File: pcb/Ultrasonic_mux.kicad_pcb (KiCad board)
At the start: 2 copper layers, 199.4 x 99.1 mm, 70 parts, among them J0 DB9_Male, J1 DB9_Male, J10 Conn_01x03_Male, J11 Conn_01x03_Male, J12 Conn_01x03_Male, J13 Conn_01x03_Male, J14 Conn_01x03_Male, J15 Conn_01x03_Male, J2 DB9_Male, J3 DB9_Male, J4 DB9_Male, J5 DB9_Male, P1 , P12 , P27 , P28 , P3 , P5 , Q0 MMBT3904, Q1 MMBT3904, Q2 MMBT3904, Q3 MMBT3904, Q4 MMBT3904, Q5 MMBT3904, U1 FeatherM0

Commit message: Organized layout.
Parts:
- moved R2 41.3 mm to (125.0, 78.7)
- moved D22 37.3 mm to (248.9, 78.2), turned to 90 degrees
- moved R3 34.6 mm to (136.1, 83.8), turned to 90 degrees
- moved D31 30.8 mm to (131.1, 135.6), turned to 270 degrees
- moved D2 30.4 mm to (136.1, 77.7), turned to 90 degrees
- moved Q0 29.5 mm to (118.4, 79.2), turned to 180 degrees
- moved R33 26.0 mm to (135.1, 130.0), turned to 270 degrees
- moved P1 23.2 mm to (112.8, 118.9)
- moved D51 23.2 mm to (243.8, 134.1), turned to 270 degrees
- moved R32 22.9 mm to (125.0, 134.1)
- moved D0 22.5 mm to (113.3, 79.2)
- moved D52 20.1 mm to (247.9, 134.6), turned to 270 degrees
- moved D32 19.3 mm to (135.1, 135.6), turned to 270 degrees
- moved D41 19.1 mm to (187.5, 135.1), turned to 270 degrees
- moved +5Vp1 19.1 mm to (119.4, 105.7)
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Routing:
- net GNDPWR: track 41.9 -> 257.1 mm
- net +3V3: track 5.18 -> 29.6 mm
- net Net-(D20-Pad1): track 0.00 -> 22.1 mm
- net Net-(D0-Pad1): track 0.00 -> 21.4 mm
- net Net-(J0-Pad2): track 0.00 -> 20.3 mm
- net Net-(J2-Pad2): track 0.00 -> 20.2 mm
- net Net-(D30-Pad1): track 0.00 -> 18.2 mm
- net Net-(J3-Pad2): track 0.00 -> 18.1 mm
- net Net-(J4-Pad2): track 0.00 -> 17.3 mm
- net Net-(D40-Pad1): track 0.00 -> 16.9 mm
- net Net-(J5-Pad2): track 0.00 -> 16.8 mm
- net Net-(D50-Pad1): track 0.00 -> 15.9 mm
- net RX0: track 0.00 -> 6.46 mm
- net Net-(D41-Pad1): track 0.00 -> 6.34 mm
- net Net-(D51-Pad1): track 0.00 -> 5.83 mm
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
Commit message: Hopefully finished track routes.
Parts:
- +3V3p1, +5Vp1, GNDp1: footprint Pin_Headers:Pin_Header_Angled_1x01_Pitch2.54mm -> Pin_Headers:Pin_Header_Straight_1x01_Pitch2.54mm
- moved GNDp1 151.6 mm to (265.2, 59.4), turned to 180 degrees
- moved +3V3p1 150.1 mm to (260.6, 59.4), turned to 180 degrees
- moved +5Vp1 144.3 mm to (256.0, 59.4), turned to 180 degrees
- moved P1 28.2 mm to (135.1, 101.6)
- moved P12 24.6 mm to (135.1, 113.8)
- moved P3 23.8 mm to (135.1, 105.7)
- moved P27 22.4 mm to (135.1, 97.5)
- moved P28 22.4 mm to (135.1, 92.5)
- moved P5 22.4 mm to (135.1, 109.7)
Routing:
- net +3V3: track 29.6 -> 605.8 mm, vias 0 -> 6
- net GNDPWR: track 257.1 -> 803.0 mm, vias 0 -> 1
- net +5V: track 0.00 -> 532.4 mm
- net RX3: track 4.76 -> 163.9 mm, vias 0 -> 2
- net TRG5: track 0.00 -> 123.5 mm, vias 0 -> 2
- net RX5: track 4.76 -> 118.1 mm, vias 0 -> 2
- net TRG3: track 0.00 -> 111.9 mm, vias 0 -> 4
- net TRG0: track 0.00 -> 110.4 mm, vias 0 -> 3
- net IND5: track 0.00 -> 106.2 mm, vias 0 -> 1
- net IND3: track 0.00 -> 101.1 mm, vias 0 -> 4
- net TRG2: track 0.00 -> 100.2 mm
- net RX0: track 6.46 -> 100.9 mm, vias 0 -> 4
- net RX2: track 5.75 -> 97.6 mm, vias 0 -> 2
- net IND2: track 0.00 -> 83.1 mm, vias 0 -> 1
- net Net-(P12-Pad1): track 0.00 -> 78.5 mm, vias 0 -> 3
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
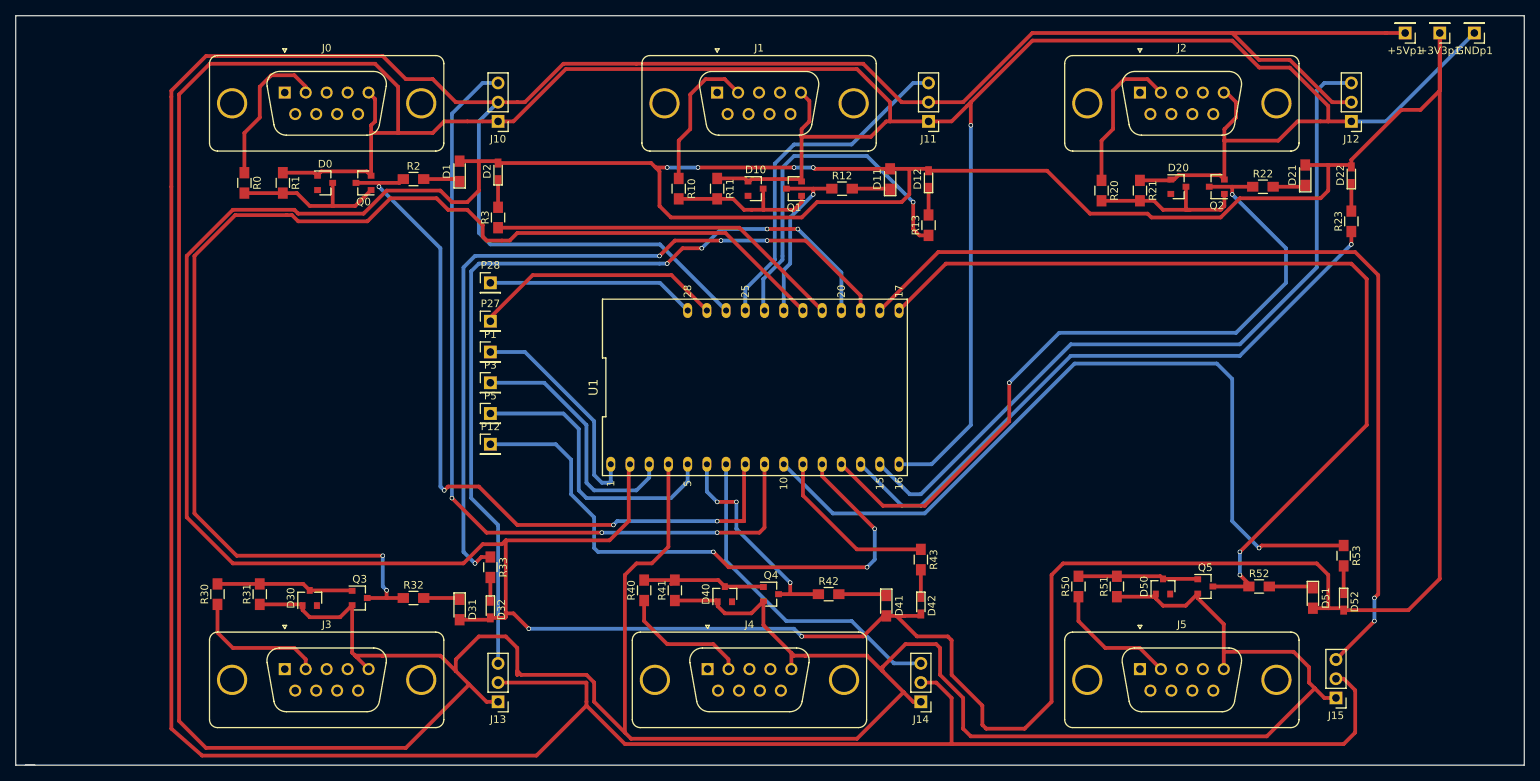
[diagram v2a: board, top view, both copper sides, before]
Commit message: BD: Reduced board size to 150x100mm for easier fit on 'bot, and reduced mechanical stress. Added vias to permit easier mods (runner cuts and soldered wire reconnect to another pad/circuit)
It still thinks 5v is not connected!
Tried replacing connecting segments to J13 and U1
Tried adding another trace to each on bottom of board
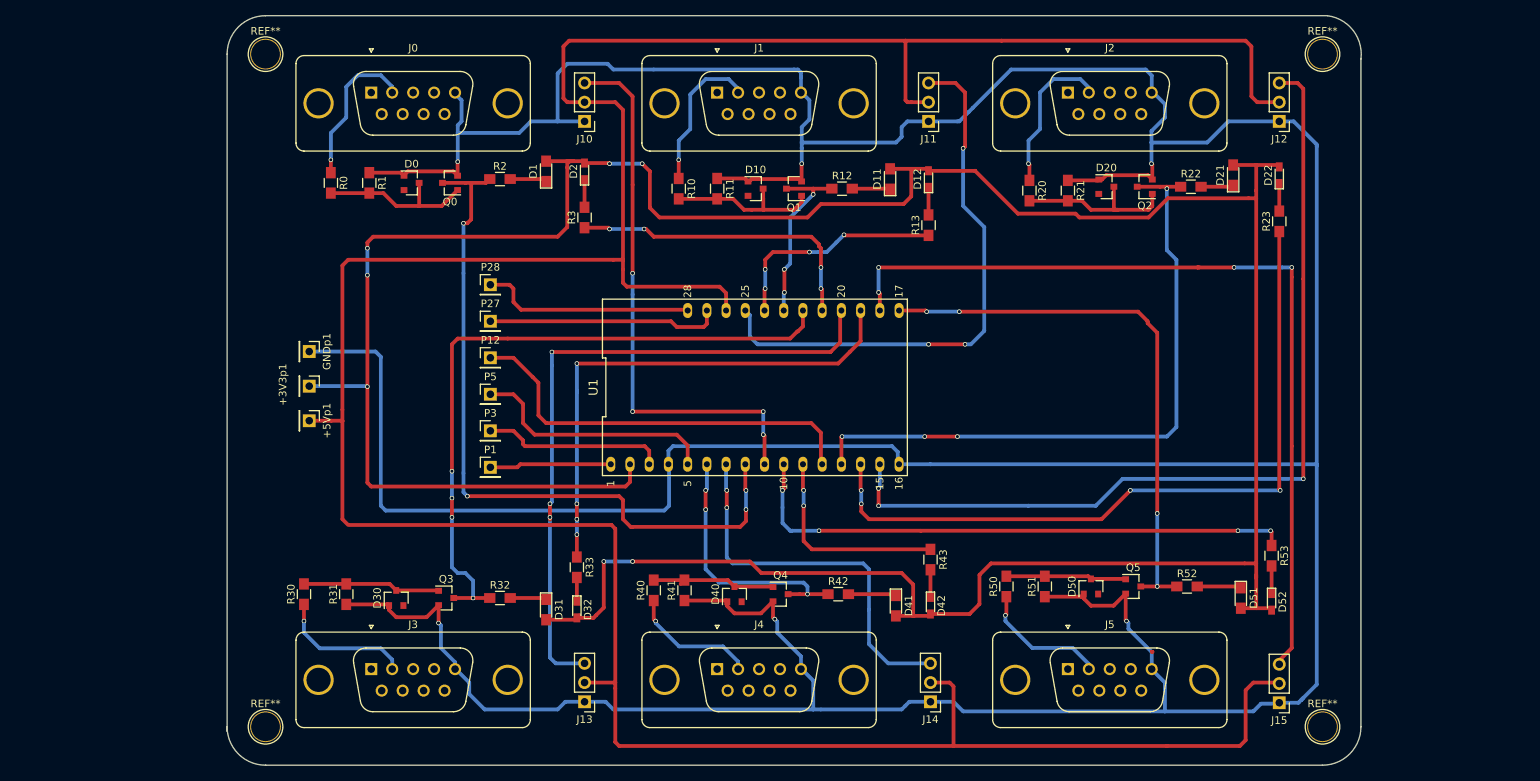
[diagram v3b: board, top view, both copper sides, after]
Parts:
- added REF**: 1pin, Connectors:1pin, F.Cu at (245.1, 151.1)
- added REF**: 1pin, Connectors:1pin, F.Cu at (105.4, 151.1)
- added REF**: 1pin, Connectors:1pin, F.Cu at (105.4, 62.2)
- added REF**: 1pin, Connectors:1pin, F.Cu at (245.1, 62.2)
- moved GNDp1 159.6 mm to (111.2, 101.5), turned to 270 degrees
- moved +3V3p1 156.5 mm to (111.2, 106.1), turned to 270 degrees
- moved +5Vp1 153.6 mm to (111.2, 110.7), turned to 270 degrees
- moved P1 15.2 mm to (135.1, 116.8)
- moved D1 11.4 mm to (142.5, 77.7)
- moved D2 11.4 mm to (147.6, 77.7)
- moved D30 11.4 mm to (122.7, 134.1)
- moved D31 11.4 mm to (142.5, 135.6)
- moved D32 11.4 mm to (146.6, 135.6)
- moved J10 11.4 mm to (147.6, 71.1)
- moved J13 11.4 mm to (147.6, 147.8)
- moved P12 11.4 mm to (135.1, 102.4)
- moved Q0 11.4 mm to (129.8, 79.2)
- moved Q3 11.4 mm to (129.3, 134.1)
- moved R0 11.4 mm to (114.0, 79.2)
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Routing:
- net +3V3: track 605.8 -> 409.0 mm, vias 6 -> 7
- net GNDPWR: track 803.0 -> 650.0 mm, vias 1 -> 6
- net +5V: track 532.4 -> 418.4 mm
- net RX3: track 163.9 -> 89.5 mm, vias 2 -> 4
- net RX5: track 118.1 -> 74.1 mm, vias 2 -> 4
- net TRG0: track 110.4 -> 73.0 mm, vias 3 -> 4
- net IND3: track 101.1 -> 68.6 mm
- net IND5: track 106.2 -> 74.8 mm, vias 1 -> 4
- net TRG1: track 45.8 -> 74.0 mm, vias 0 -> 3
- net Net-(P12-Pad1): track 78.5 -> 54.6 mm, vias 3 -> 0
- net TRG3: track 111.9 -> 88.6 mm, vias 4 -> 3
- net TRG2: track 100.2 -> 118.2 mm, vias 0 -> 3
- net IND1: track 46.4 -> 30.0 mm, vias 1 -> 4
- net IND2: track 83.1 -> 97.9 mm, vias 1 -> 4
- net Net-(P1-Pad1): track 29.6 -> 16.1 mm
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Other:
- board size 199.4 x 99.1 mm -> 149.9 x 99.1 mm

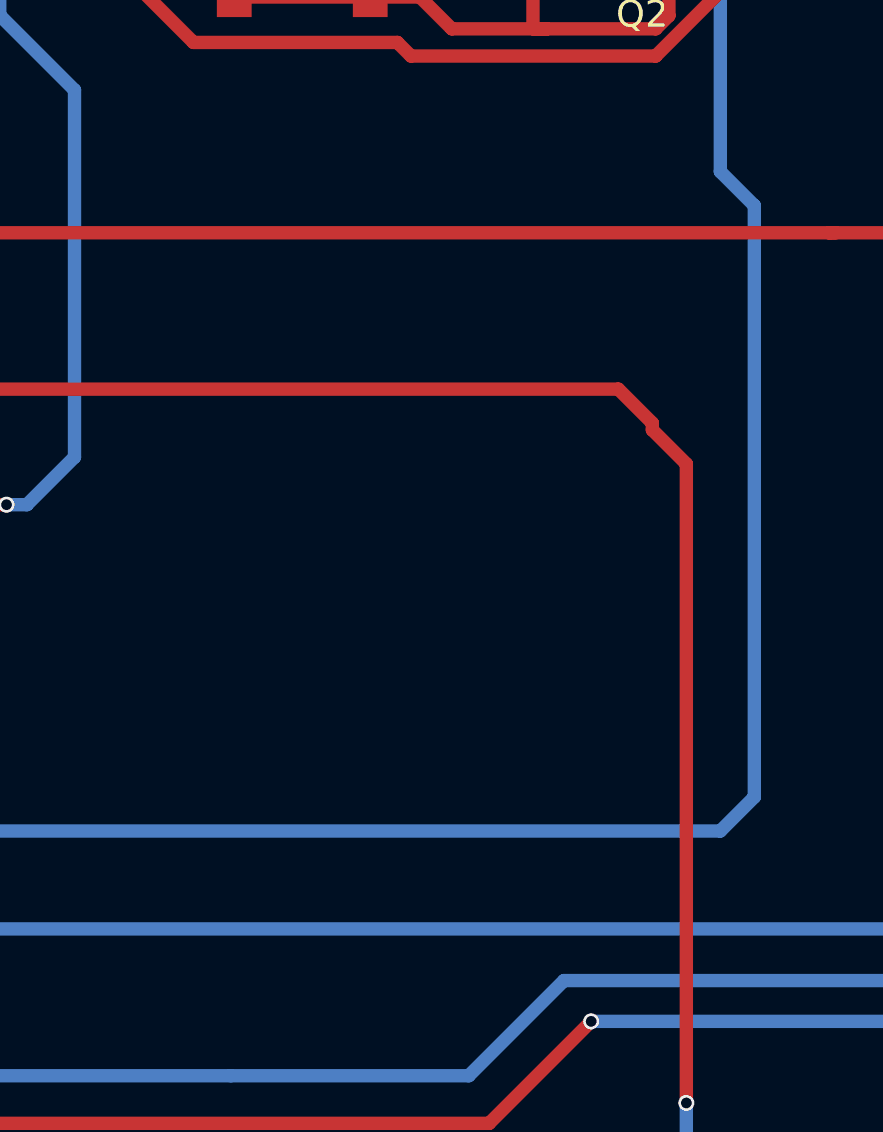
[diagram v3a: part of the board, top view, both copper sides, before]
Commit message: Added logo and text Still an issue with the 5v connection Order is based on gerber's, so shouldn't be a problem Worst case, small jumper wire Created gerber files
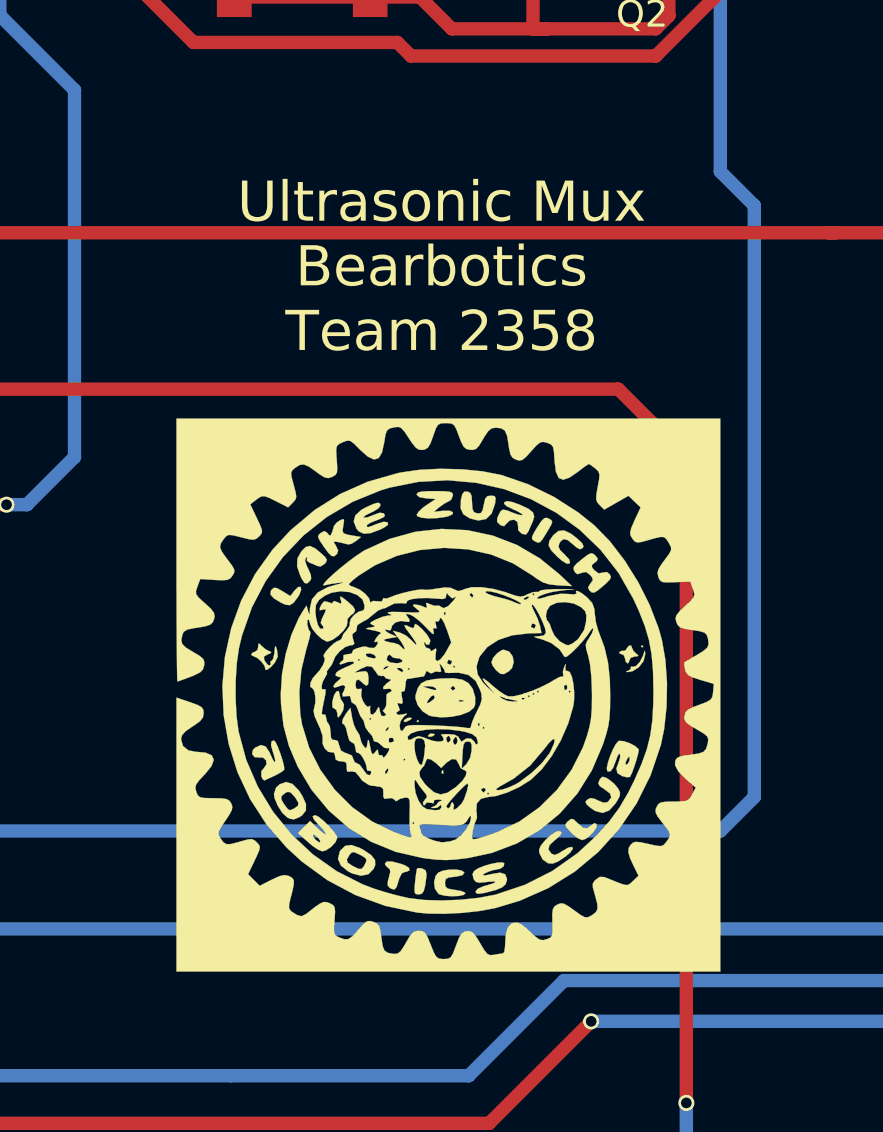
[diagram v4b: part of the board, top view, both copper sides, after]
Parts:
- added G***: LOGO, Tech Club Logo:tech_club_logo, F.Cu at (214.4, 107.7)
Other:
- board text added: "Ultrasonic Mux Bearbotics Team 2358"
